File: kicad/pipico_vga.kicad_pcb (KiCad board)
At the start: 2 copper layers, 50 x 96 mm, 66 parts, among them J1 RJ45_LED_Shielded, J2 DB15_Male_HighDensity_Mountin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, J3 power, Q1 2N7002P, Q2 2N7002P, Q3 CPH3350-TL-W, U1 Pico, U2 74LVC162244ADGVJ, U3 AP62250

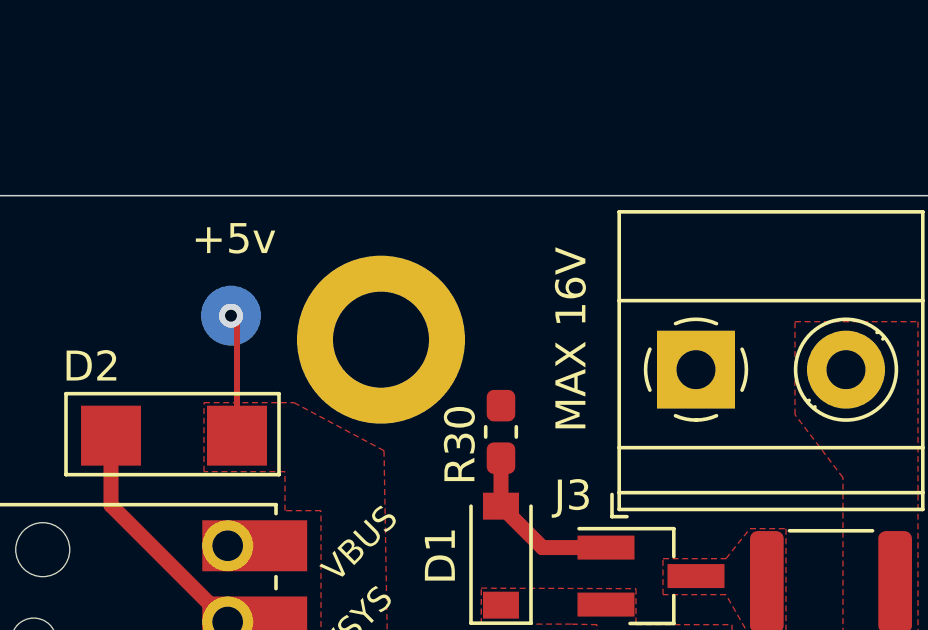
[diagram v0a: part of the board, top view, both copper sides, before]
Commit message: Start make controller
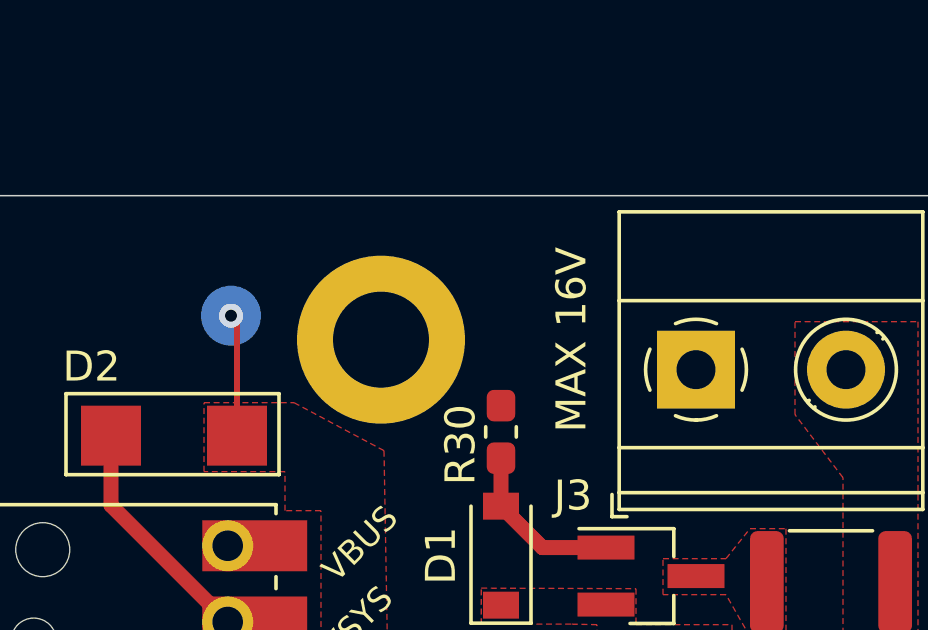
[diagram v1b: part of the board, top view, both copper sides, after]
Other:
- net class Default removed

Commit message: Rev 4 of main board
controller rev1 done as well :D
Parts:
- removed Q1, Q2: 2N7002P, Package_TO_SOT_SMD:SOT-23_Handsoldering
- added C10: 4u7, Capacitor_SMD:C_0603_1608Metric_Pad1.08x0.95mm_HandSolder, B.Cu at (157.5, 90.2)
- added C11: 100n, Capacitor_SMD:C_0603_1608Metric_Pad1.08x0.95mm_HandSolder, F.Cu at (146.6, 99.1)
- added C9: 4u7, Capacitor_SMD:C_0603_1608Metric_Pad1.08x0.95mm_HandSolder, B.Cu at (157.5, 110.2)
- added H5: MountingHole_Pad, MountingHole:MountingHole_3.2mm_M3_DIN965_Pad, F.Cu at (163.0, 68.2)
- added J4: RJE37-188-2410, Connector_RJ:RJ45_Amphenol_RJHSE538X, F.Cu at (158.4, 101.1)
- added R33: 10k, Resistor_SMD:R_0603_1608Metric_Pad0.98x0.95mm_HandSolder, F.Cu at (135.0, 87.2)
- added R34: 10k, Resistor_SMD:R_0603_1608Metric_Pad0.98x0.95mm_HandSolder, F.Cu at (135.0, 90.8)
- added R35: 1k, Resistor_SMD:R_0603_1608Metric_Pad0.98x0.95mm_HandSolder, F.Cu at (149.0, 79.3)
- added R36: 1k, Resistor_SMD:R_0603_1608Metric_Pad0.98x0.95mm_HandSolder, F.Cu at (149.0, 110.7)
- added U4: PI3C3305LE, Package_SO:TSSOP-8_4.4x3mm_P0.65mm, F.Cu at (145.5, 93.2)
- C1, C2, C3, C4, C6, C7, C8: footprint Capacitor_SMD:C_0603_1608Metric_Pad1.05x0.95mm_HandSolder -> Capacitor_SMD:C_0603_1608Metric_Pad1.08x0.95mm_HandSolder
- J1: value RJ45_LED_Shielded -> RJE37-188-2410; footprint Connector_RJ:RJ45_BEL_SS74301-00x_Vertical -> Connector_RJ:RJ45_Amphenol_RJHSE538X
- R1, R10, R11, R12, R13, R14, R15, R16, R17, R18, R19, R2, R20, R21, R22, R23, R24, R25, R26, R27, R28, R29, R3, R30, R31, R32, R4, R5, R6, R7, R8, R9: footprint Resistor_SMD:R_0603_1608Metric_Pad1.05x0.95mm_HandSolder -> Resistor_SMD:R_0603_1608Metric_Pad0.98x0.95mm_HandSolder
- moved J1 22.1 mm to (158.5, 81.2), turned to -90 degrees
- moved H1 21.4 mm to (163.0, 121.2)
- moved R29 16.0 mm to (149.0, 99.2), turned to -90 degrees
- moved R28 8.97 mm to (148.8, 90.7), turned to -90 degrees
- moved H3 4.20 mm to (115.0, 121.2)
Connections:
- J1 pad 1: tx -> /dshift
- J1 pad 10: +3V3 -> Net-(J1-Pad10)
- J1 pad 11: Net-(J1-Pad11) -> /connected_0_n
- J1 pad 12: +3V3 -> Net-(J1-Pad12)
- J1 pad 2: rx -> /clk
- J1 pad 3: +3V3 -> /out_shift_clk
- J1 pad 4: (no net) -> /ie_n
- J1 pad 5: (no net) -> /connected_0_n
- J1 pad 6: (no net) -> /copi
- J1 pad 7: connected -> GND
- J1 pad 8: GND -> +3V3
- J1 pad 9: Net-(J1-Pad9) -> GND
- J2 pad 11: (no net) -> unconnected-(J2-Pad11)
- J2 pad 4: (no net) -> unconnected-(J2-Pad4)
- J2 pad 9: (no net) -> unconnected-(J2-Pad9)
- R28 pad 1: Net-(J1-Pad11) -> +3V3
- R28 pad 2: Net-(Q2-Pad3) -> Net-(J1-Pad12)
- R29 pad 1: Net-(J1-Pad9) -> +3V3
- U1 pad 20: Net-(U1-Pad20) -> unconnected-(U1-Pad20)
- U1 pad 21: tx -> /cipo
- U1 pad 22: rx -> /out_shift_clk
- U1 pad 24: /vga_data -> /clk
- U1 pad 25: /vga_clk -> /copi
- U1 pad 26: connected -> unconnected-(U1-Pad26)
- U1 pad 27: /led1 -> /connected_1_n
- U1 pad 29: /led0 -> /connected_0_n
- U1 pad 30: Net-(U1-Pad30) -> unconnected-(U1-Pad30)
- U1 pad 31: Net-(U1-Pad31) -> /vga_data
- U1 pad 32: Net-(U1-Pad32) -> /vga_clk
- U1 pad 34: Net-(U1-Pad34) -> /ie_n
- U1 pad 35: Net-(U1-Pad35) -> unconnected-(U1-Pad35)
- U1 pad 37: Net-(U1-Pad37) -> unconnected-(U1-Pad37)
- U1 pad 40: Net-(U1-Pad40) -> unconnected-(U1-Pad40)
- U2 pad 37: (no net) -> unconnected-(U2-Pad37)
- U2 pad 38: (no net) -> unconnected-(U2-Pad38)
- U2 pad 40: (no net) -> unconnected-(U2-Pad40)
- U2 pad 41: (no net) -> unconnected-(U2-Pad41)
- U3 pad 5: (no net) -> unconnected-(U3-Pad5)
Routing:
- net /out_shift_clk: track 0.00 -> 59.1 mm, vias 0 -> 1
- net /cipo: track 0.00 -> 52.7 mm
- net /dshift: track 0.00 -> 48.2 mm, vias 0 -> 1
- net /ie_n: track 0.00 -> 47.2 mm, vias 0 -> 1
- net /clk: track 0.00 -> 43.6 mm, vias 0 -> 1
- net /connected_1_n: track 0.00 -> 41.4 mm, vias 0 -> 3
- net /connected_0_n: track 0.00 -> 39.0 mm
- net /copi: track 0.00 -> 36.1 mm, vias 0 -> 3
- net /led0: track 26.0 -> 0.00 mm
- net Net-(J1-Pad11): track 23.5 -> 0.00 mm
- net /led1: track 22.0 -> 0.00 mm
- net /vga_data: track 55.0 -> 73.4 mm
- net connected: track 16.2 -> 0.00 mm
- net tx: track 15.4 -> 0.00 mm
- net /vga_clk: track 74.4 -> 86.7 mm
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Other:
- board size 50 x 96 mm -> 56 x 96 mm
- board text added: "PLAYER 0"
- board text added: "PLAYER 1"
- board text added: "Raspberry Pi PICO VGA rev4 Anton Lööf 2022"
- board text removed: "PLAYER"
- board text removed: "Raspberry Pi PICO VGA Anton Lööf 2021 rev3"

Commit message: rev4 main and rev1 controller ready for order
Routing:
- net /hsync: track 49.8 -> 50.4 mm
